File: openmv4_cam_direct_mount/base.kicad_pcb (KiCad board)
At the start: 4 copper layers, 36 x 34 mm, 57 parts, among them Q1 BSS138, Q2 Si2301BDS, U1 STM32H743VIT6, U2 OV7725, U5 TPS731XX, U8 PAM2305AABADJ, X1 MF-CON-MICROUSB-RIGHT, X2 USD-1040310811, Y1 7S-12.000MAHE-T

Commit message: Added connector to schematic
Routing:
- net /TIM4_CH3: track 14.2 -> 1.63 mm, vias 2 -> 1
- net /DCMI_D0: track 0.59 -> 12.7 mm, vias 2 -> 3
- net /DCMI_CLK: track 2.30 -> 12.8 mm, vias 2 -> 3
- net /DCMI_D1: track 0.58 -> 10.8 mm
- net /FSIN: track 9.60 -> 0.00 mm
- net /DCMI_D7: track 9.74 -> 14.5 mm, vias 1 -> 3
- net /SPI3_SSEL: track 0.99 -> 0.00 mm
- net /SD_CD: track 15.6 -> 16.4 mm

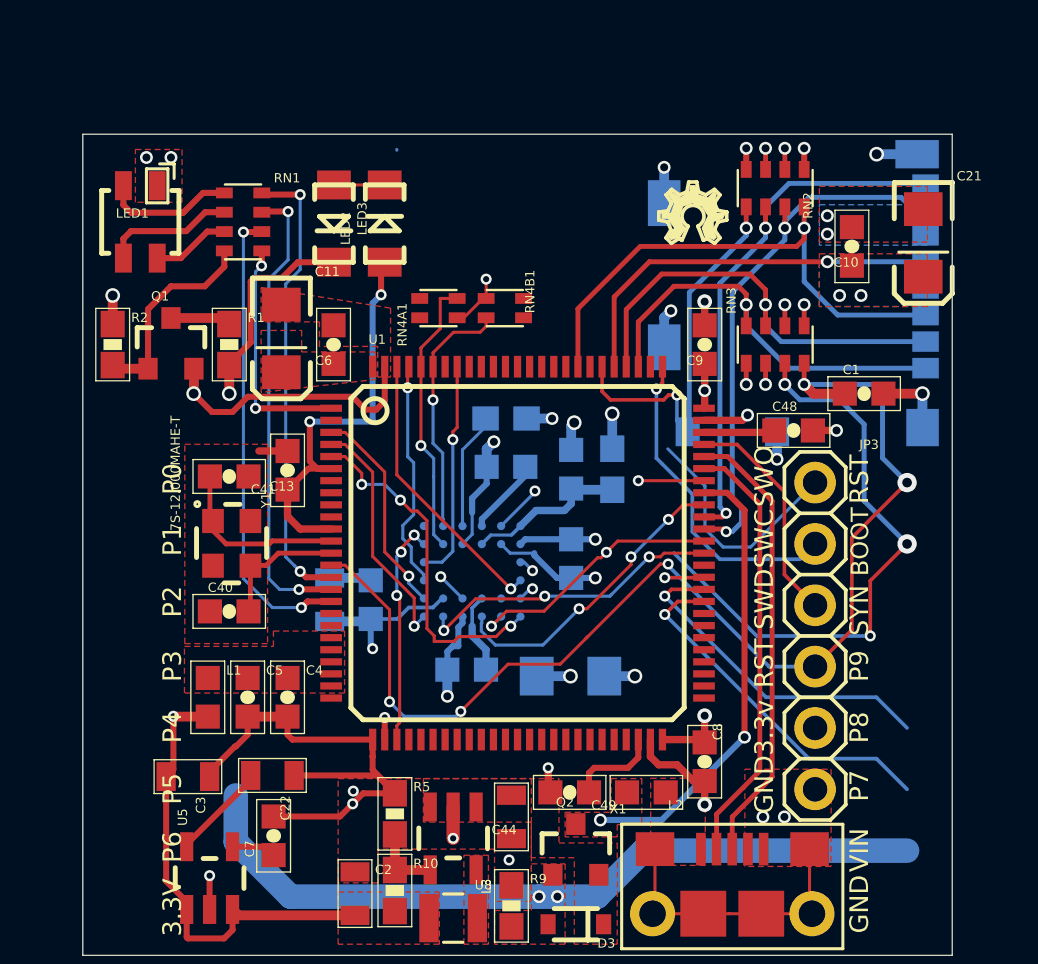
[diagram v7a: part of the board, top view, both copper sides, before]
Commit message: Finished connecting main components
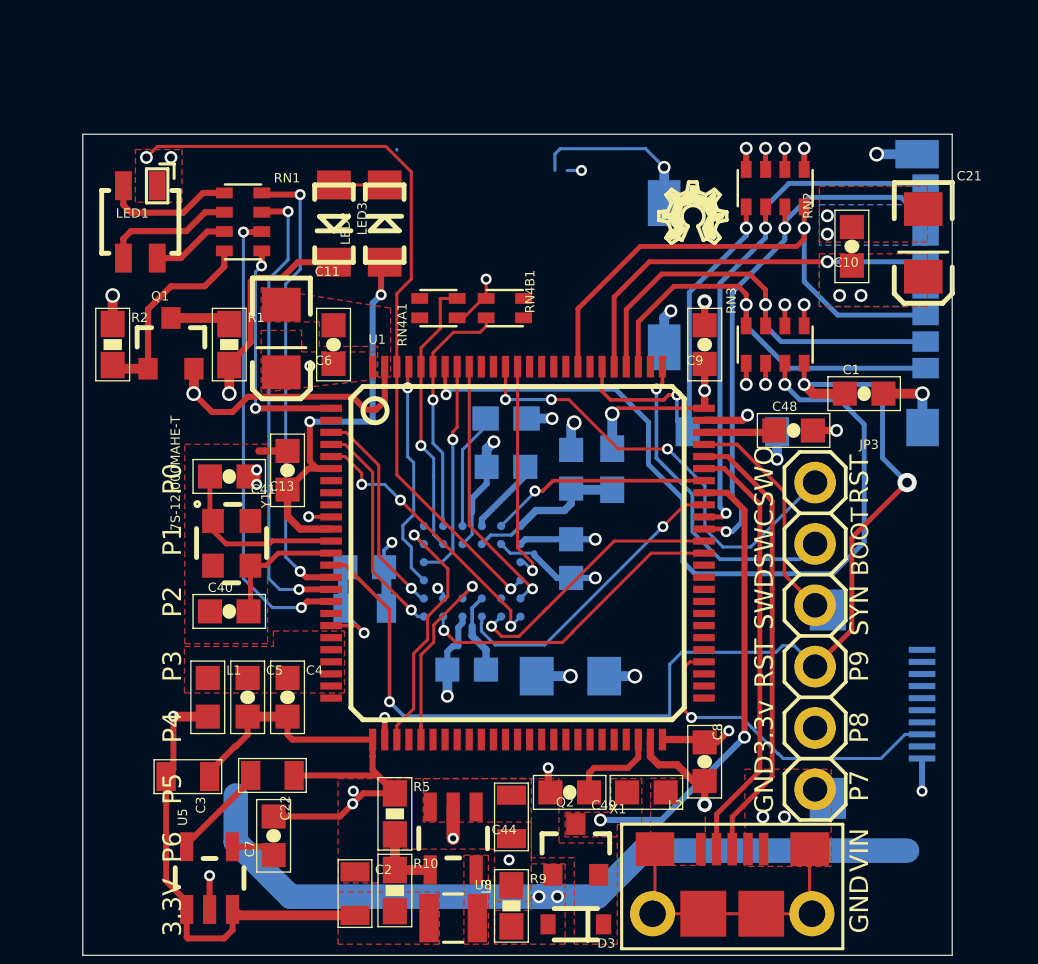
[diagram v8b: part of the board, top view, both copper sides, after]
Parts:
- added J5: XF2M-1015-1A, XF2M-1015-1A:XF2M-1015-1A, B.Cu at (165.2, 117.1)
- moved C20 1.49 mm to (142.2, 113.1), turned to 180 degrees
- moved C19 1.37 mm to (142.2, 111.4), turned to 180 degrees
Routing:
- net /DCMI_D3: track 11.7 -> 31.6 mm
- net /TIM4_CH1: track 14.9 -> 0.00 mm, vias 1 -> 0
- net /TIM4_CH2: track 14.0 -> 0.00 mm, vias 1 -> 0
- net /SPI2_MOSI: track 0.00 -> 13.7 mm, vias 0 -> 1
- net /DCMI_D5: track 0.67 -> 10.9 mm
- net /BOOT0: track 24.5 -> 34.6 mm, vias 3 -> 2
- net GND: track 74.2 -> 83.5 mm, vias 28 -> 32
- net /SPI3_SCLK/TRACESWO: track 9.93 -> 18.9 mm, vias 0 -> 3
- net /DCMI_PWDN: track 0.64 -> 9.35 mm
- net /DCMI_PCLK: track 1.28 -> 8.48 mm
- net /DCMI_RST: track 4.75 -> 9.21 mm, vias 2 -> 1
- net /DCMI_D7: track 14.5 -> 11.6 mm
- net VCC: track 59.4 -> 62.3 mm, vias 20 -> 24
- net /NRST: track 49.1 -> 47.3 mm, vias 5 -> 3
- net /TIM4_CH3: track 1.63 -> 0.02 mm, vias 1 -> 0
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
